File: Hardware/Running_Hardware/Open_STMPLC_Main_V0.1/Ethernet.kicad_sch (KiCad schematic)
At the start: 19 parts, among them J11 HY951180A, U7 LAN8720A, Y3 25MHz

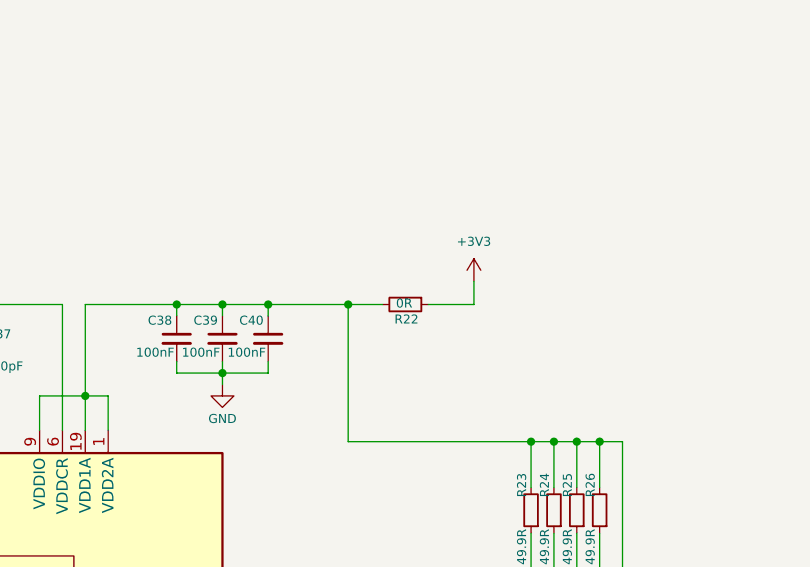
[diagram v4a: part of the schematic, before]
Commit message: Schematic updates
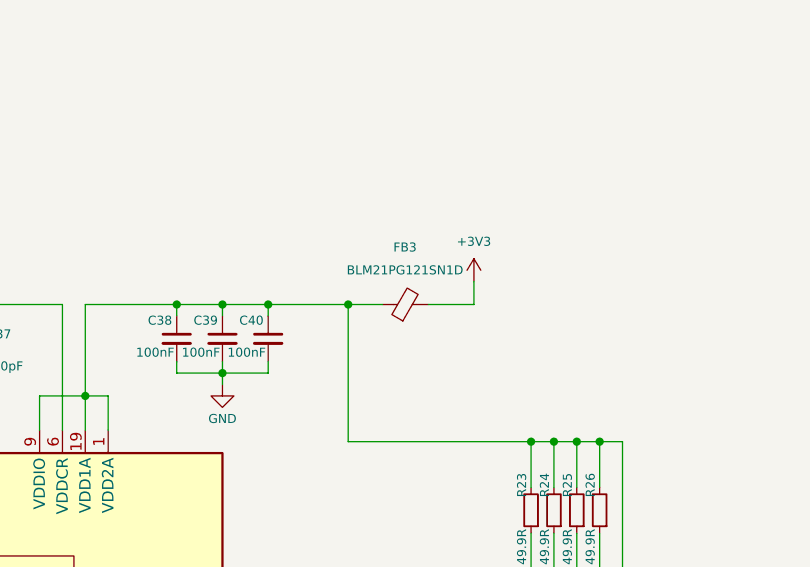
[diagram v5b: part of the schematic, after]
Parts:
- removed R22: 0R, Resistor_SMD:R_0603_1608Metric_Pad0.98x0.95mm_HandSolder, symbol Device:R_Small
- added FB3: BLM21PG121SN1D, Inductor_SMD:L_0805_2012Metric_Pad1.05x1.20mm_HandSolder, symbol Device:FerriteBead_Small
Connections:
- net +3V3: now also FB3.2
- net at C38.1, C39.1, C40.1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: now also FB3.1
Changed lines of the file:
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@@
+			)
+		)
+		(property "Sim.Pin" ""
+			(at 64.77 130.81 90)
+			(effects
+				(font
+					(size 1.27 1.27)
+				)
+				(hide yes)
 			)
 		)
@@
 			)
 		)
+		(property "Sim.Pin" ""
+			(at 127 58.42 0)
+			(effects
+				(font
+					(size 1.27 1.27)
+				)
+				(hide yes)
+			)
+		)
 		(pin "1"
 		)
@@
 		)
 		(property "Description" "Unpolarized capacitor, small symbol"
+			(at 95.25 59.69 0)
+			(effects
+				(font
+					(size 1.27 1.27)
+				)
+				(hide yes)
+			)
+		)
+		(property "Sim.Pin" ""
 			(at 95.25 59.69 0)
 			(effects
@@
 			)
 		)
+		(property "Sim.Pin" ""
+			(at 200.66 93.98 0)
+			(effects
+				(font
+					(size 1.27 1.27)
+				)
+				(hide yes)
+			)
+		)
 		(pin "6"
 		)
@@
 		(property "Description" "Resistor, small symbol"
 			(at 232.41 82.55 0)
+			(effects
+				(font
+					(size 1.27 1.27)
+				)
+				(hide yes)
+			)
+		)
+		(property "Sim.Pin" ""
+			(at 232.41 82.55 90)
 			(effects
 				(font
@@
 	)
 	(symbol
+		(lib_id "Device:FerriteBead_Small")
+		(at 147.32 54.61 90)
+		(unit 1)
+		(exclude_from_sim no)
+		(in_bom yes)
+		(on_board yes)
+		(dnp no)
+		(fields_autoplaced yes)
+		(property "Reference" "FB3"
+			(at 147.2819 48.26 90)
+			(effects
+				(font
+					(size 1 1)
+				)
+			)
+		)
+		(property "Value" "BLM21PG121SN1D"
+			(at 147.2819 50.8 90)
+			(effects
+				(font
+					(size 1 1)
+				)
+			)
+		)
+		(property "Footprint" "Inductor_SMD:L_0805_2012Metric_Pad1.05x1.20mm_HandSolder"
+			(at 147.32 56.388 90)
+			(effects
+				(font
+					(size 1.27 1.27)
+				)
+				(hide yes)
+			)
+		)
+		(property "Datasheet" "~"
+			(at 147.32 54.61 0)
+			(effects
+				(font
+					(size 1.27 1.27)
+				)
+				(hide yes)
+			)
+		)
+		(property "Description" "Ferrite bead, small symbol"
+			(at 147.32 54.61 0)
+			(effects
+				(font
+					(size 1.27 1.27)
+				)
+				(hide yes)
+			)
+		)
+		(pin "1"
+		)
+		(pin "2"
+		)
+		(instances
+			(project "Open_STMPLC_Main_V0.1"
+				(path "/0b17c9ff-697e-478a-b9b2-a0c5b14c9e6c/2c4ca765-43c3-4f95-8835-dba7f06999bb"
+					(reference "FB3")
+					(unit 1)
+				)
+			)
+		)
+	)
+	(symbol
 		(lib_id "Device:R_Small")
 		(at 168.91 77.47 180)
@@
 			)
 		)
+		(property "Sim.Pin" ""
+			(at 168.91 77.47 90)
+			(effects
+				(font
+					(size 1.27 1.27)
+				)
+				(hide yes)
+			)
+		)
 		(pin "2"
 		)
@@
 			)
 		)
+		(property "Sim.Pin" ""
+			(at 133.35 101.6 90)
+			(effects
+				(font
+					(size 1.27 1.27)
+				)
+				(hide yes)
+			)
+		)
 		(pin "2"
 		)
@@
 				(path "/0b17c9ff-697e-478a-b9b2-a0c5b14c9e6c/2c4ca765-43c3-4f95-8835-dba7f06999bb"
 					(reference "R21")
-					(unit 1)
-				)
-			)
-		)
-	)
-	(symbol
-		(lib_id "Device:R_Small")
-		(at 147.32 54.61 270)
-		(unit 1)
-		(exclude_from_sim no)
-		(in_bom yes)
-		(on_board yes)
-		(dnp no)
-		(property "Reference" "R22"
-			(at 147.447 56.261 90)
-			(effects
-				(font
-					(size 1 1)
-				)
-			)
-		)
-		(property "Value" "0R"
-			(at 147.193 54.483 90)
-			(effects
-				(font
-					(size 1 1)
-				)
-			)
-		)
-		(property "Footprint" "Resistor_SMD:R_0603_1608Metric_Pad0.98x0.95mm_HandSolder"
-			(at 147.32 54.61 0)
-			(effects
-				(font
-					(size 1.27 1.27)
-				)
-				(hide yes)
-			)
-		)
-		(property "Datasheet" "~"
-			(at 147.32 54.61 0)
-			(effects
-				(font
-					(size 1.27 1.27)
-				)
-				(hide yes)
-			)
-		)
-		(property "Description" "Resistor, small symbol"
-			(at 147.32 54.61 0)
-			(effects
-				(font
-					(size 1.27 1.27)
-				)
-				(hide yes)
-			)
-		)
-		(pin "2"
-		)
-		(pin "1"
-		)
-		(instances
-			(project "Open_STMPLC_Main_V0.1"
-				(path "/0b17c9ff-697e-478a-b9b2-a0c5b14c9e6c/2c4ca765-43c3-4f95-8835-dba7f06999bb"
-					(reference "R22")
 					(unit 1)
 				)
@@
 		(property "Description" "Resistor, small symbol"
 			(at 161.29 77.47 0)
+			(effects
+				(font
+					(size 1.27 1.27)
+				)
+				(hide yes)
+			)
+		)
+		(property "Sim.Pin" ""
+			(at 161.29 77.47 90)
 			(effects
 				(font
@@
 			)
 		)
+		(property "Sim.Pin" ""
+			(at 132.08 58.42 0)
+			(effects
+				(font
+					(size 1.27 1.27)
+				)
+				(hide yes)
+			)
+		)
 		(pin "1"
 		)
@@
 		(property "Description" "Resistor, small symbol"
 			(at 163.83 77.47 0)
+			(effects
+				(font
+					(size 1.27 1.27)
+				)
+				(hide yes)
+			)
+		)
+		(property "Sim.Pin" ""
+			(at 163.83 77.47 90)
 			(effects
 				(font
@@
 			)
 		)
+		(property "Sim.Pin" ""
+			(at 171.45 105.41 0)
+			(effects
+				(font
+					(size 1.27 1.27)
+				)
+				(hide yes)
+			)
+		)
 		(pin "1"
 		)
@@
 			)
 		)
+		(property "Sim.Pin" ""
+			(at 111.76 99.06 0)
+			(effects
+				(font
+					(size 1.27 1.27)
+				)
+				(hide yes)
+			)
+		)
 		(pin "18"
 		)
@@
 			)
 		)
+		(property "Sim.Pin" ""
+			(at 121.92 58.42 0)
+			(effects
+				(font
+					(size 1.27 1.27)
+				)
+				(hide yes)
+			)
+		)
 		(pin "1"
 		)
@@
 			)
 		)
+		(property "Sim.Pin" ""
+			(at 100.33 59.69 0)
+			(effects
+				(font
+					(size 1.27 1.27)
+				)
+				(hide yes)
+			)
+		)
 		(pin "1"
 		)
@@
 		(property "Description" "Resistor, small symbol"
 			(at 166.37 77.47 0)
+			(effects
+				(font
+					(size 1.27 1.27)
+				)
+				(hide yes)
+			)
+		)
+		(property "Sim.Pin" ""
+			(at 166.37 77.47 90)
 			(effects
 				(font
@@
 			)
 		)
+		(property "Sim.Pin" ""
+			(at 64.77 116.84 90)
+			(effects
+				(font
+					(size 1.27 1.27)
+				)
+				(hide yes)
+			)
+		)
 		(pin "1"
 		)
@@
 			)
 		)
+		(property "Sim.Pin" ""
+			(at 227.33 82.55 90)
+			(effects
+				(font
+					(size 1.27 1.27)
+				)
+				(hide yes)
+			)
+		)
 		(pin "2"
 		)
@@
 			(effects
 				(font
+					(size 1.27 1.27)
+				)
+				(hide yes)
+			)
+		)
+		(property "Sim.Pin" ""
+			(at 69.85 124.46 90)
+			(effects
+				(font

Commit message: Component placement main pcb
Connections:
- net ETH_~{INT} renamed ETH_REFCLKO
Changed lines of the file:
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@@
 		)
 	)
-	(hierarchical_label "ETH_~{INT}"
+	(hierarchical_label "ETH_REFCLKO"
 		(shape output)
 		(at 90.17 111.76 180)

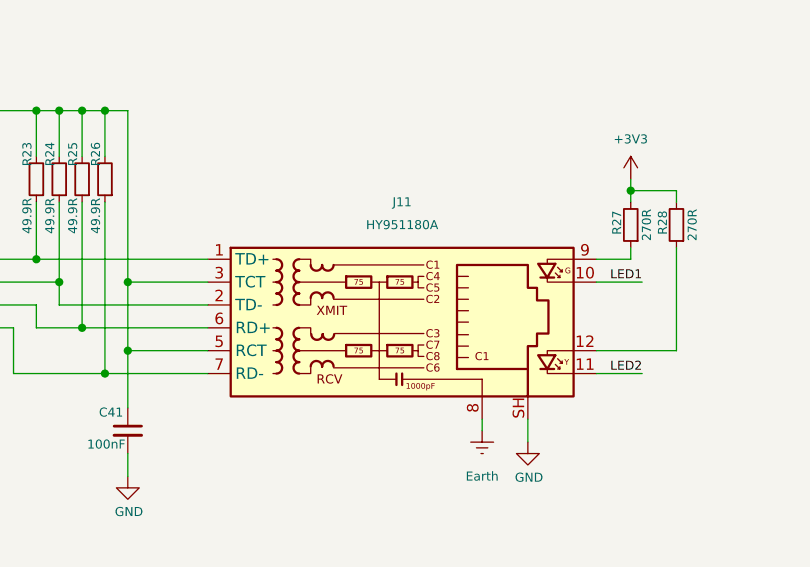
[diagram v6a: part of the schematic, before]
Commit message: IO board layout completion and DRC clear
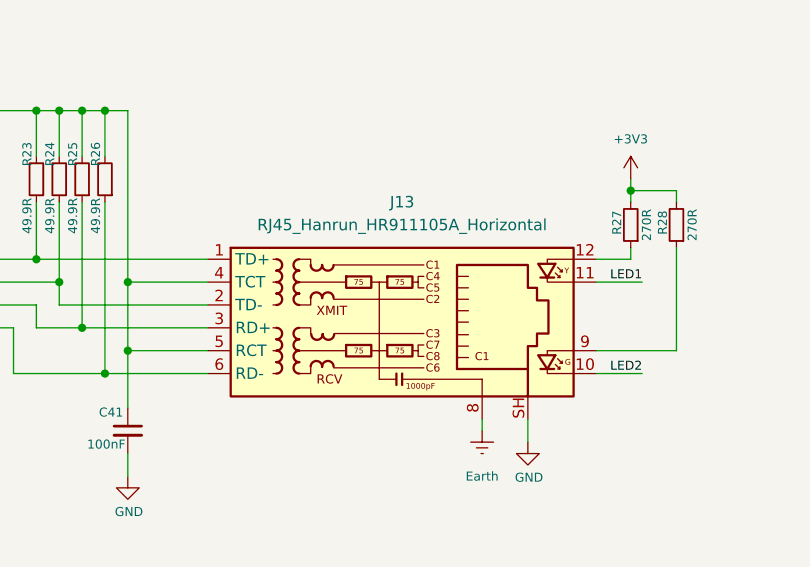
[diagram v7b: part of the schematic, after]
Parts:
- removed J11: HY951180A, HY951180A:HY951180A, symbol HY951180A:HY951180A
- added J13: RJ45_Hanrun_HR911105A_Horizontal, Connector_RJ:RJ45_Hanrun_HR911105A_Horizontal, symbol Connector:RJ45_Hanrun_HR911105A_Horizontal
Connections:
- net Earth: now also J13.8
- net GND: now also J13.SH
- net LED1: now also J13.11
- net LED2: now also J13.10
- net at C38.1, C39.1, C40.1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: now also J13.4 (TCT), J13.5 (RCT)
- net at R23.1, U7.21 (TXP): now also J13.1 (TD+)
- net at R28.1: now also J13.9
- net at R24.1, U7.20 (TXN): now also J13.2 (TD-)
- net at R25.1, U7.23 (RXP): now also J13.3 (RD+)
- net at R26.1, U7.22 (RXN): now also J13.6 (RD-)
- net at R27.1: now also J13.12
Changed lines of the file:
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@@
-	)
-	(symbol
-		(lib_id "HY951180A:HY951180A")
-		(at 200.66 93.98 0)
-		(unit 1)
-		(exclude_from_sim no)
-		(in_bom yes)
-		(on_board yes)
-		(dnp no)
-		(fields_autoplaced yes)
-		(property "Reference" "J11"
-			(at 201.93 80.01 0)
-			(effects
-				(font
-					(size 1 1)
-				)
-			)
-		)
-		(property "Value" "HY951180A"
-			(at 201.93 82.55 0)
-			(effects
-				(font
-					(size 1 1)
-				)
-			)
-		)
-		(property "Footprint" "HY951180A:HY951180A"
-			(at 200.66 81.28 0)
-			(effects
-				(font
-					(size 1.27 1.27)
-				)
-				(hide yes)
-			)
-		)
-		(property "Datasheet" ""
-			(at 200.66 78.74 0)
-			(effects
-				(font
-					(size 1.27 1.27)
-				)
-				(hide yes)
-			)
-		)
-		(property "Description" ""
-			(at 200.66 93.98 0)
-			(effects
-				(font
-					(size 1.27 1.27)
-				)
-				(hide yes)
-			)
-		)
-		(property "Sim.Pin" ""
-			(at 200.66 93.98 0)
-			(effects
-				(font
-					(size 1.27 1.27)
-				)
-				(hide yes)
-			)
-		)
-		(pin "6"
-		)
-		(pin "7"
-		)
-		(pin "2"
-		)
-		(pin "5"
-		)
-		(pin "9"
-		)
-		(pin "1"
-		)
-		(pin "11"
-		)
-		(pin "10"
-		)
-		(pin "3"
-		)
-		(pin "12"
-		)
-		(pin "8"
-		)
-		(pin "SH"
-		)
-		(pin "4"
-		)
-		(instances
-			(project "Open_STMPLC_Main_V0.1"
-				(path "/0b17c9ff-697e-478a-b9b2-a0c5b14c9e6c/2c4ca765-43c3-4f95-8835-dba7f06999bb"
-					(reference "J11")
-					(unit 1)
-				)
-			)
-		)
 	)
 	(symbol
@@
 					(unit 1)
 				)
+			)
+		)
+	)
+	(symbol
+		(lib_id "Connector:RJ45_Hanrun_HR911105A_Horizontal")
+		(at 200.66 93.98 0)
+		(unit 1)
+		(exclude_from_sim no)
+		(in_bom yes)
+		(on_board yes)
+		(dnp no)
+		(fields_autoplaced yes)
+		(property "Reference" "J13"
+			(at 201.93 80.01 0)
+			(effects
+				(font
+					(size 1.27 1.27)
+				)
+			)
+		)
+		(property "Value" "RJ45_Hanrun_HR911105A_Horizontal"
+			(at 201.93 82.55 0)
+			(effects
+				(font
+					(size 1.27 1.27)
+				)
+			)
+		)
+		(property "Footprint" "Connector_RJ:RJ45_Hanrun_HR911105A_Horizontal"
+			(at 200.66 81.28 0)
+			(effects
+				(font
+					(size 1.27 1.27)
+				)
+				(hide yes)
+			)
+		)
+		(property "Datasheet" "https://datasheet.lcsc.com/lcsc/1811141815_HANRUN-Zhongshan-HanRun-Elec-HR911105A_C12074.pdf"
+			(at 200.66 78.74 0)
+			(effects
+				(font
+					(size 1.27 1.27)
+				)
+				(hide yes)
+			)
+		)
+		(property "Description" "1 Port RJ45 Magjack Connector Through Hole 10/100 Base-T, AutoMDIX"
+			(at 200.66 93.98 0)
+			(effects
+				(font
+					(size 1.27 1.27)
+				)
+				(hide yes)
+			)
+		)
+		(pin "12"
+		)
+		(pin "9"
+		)
+		(pin "7"
+		)
+		(pin "3"
+		)
+		(pin "2"
+		)
+		(pin "6"
+		)
+		(pin "SH"
+		)
+		(pin "11"
+		)
+		(pin "5"
+		)
+		(pin "10"
+		)
+		(pin "1"
+		)
+		(pin "8"
+		)
+		(pin "4"
+		)
+		(instances
+			(project ""
+				(path "/0b17c9ff-697e-478a-b9b2-a0c5b14c9e6c/2c4ca765-43c3-4f95-8835-dba7f06999bb"
+					(reference "J13")
+					(unit 1)
+				)

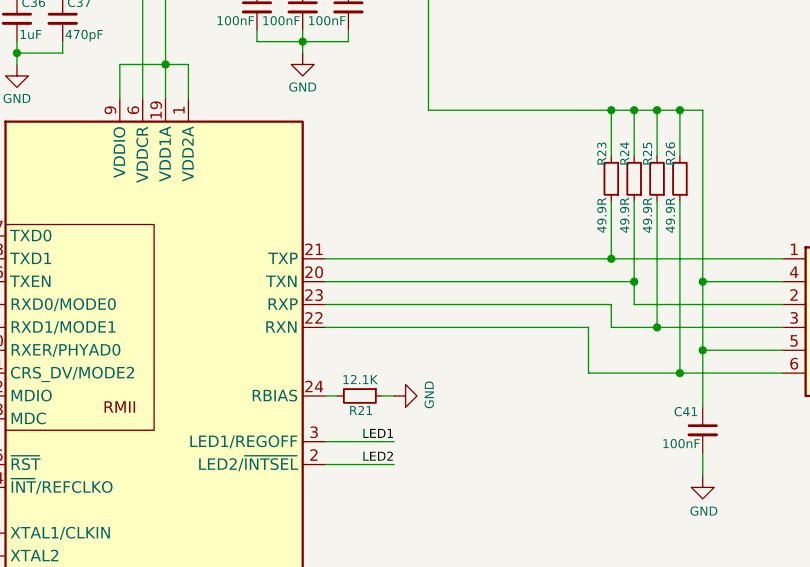
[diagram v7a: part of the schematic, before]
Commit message: Layer stack up main PCB and pin mapping
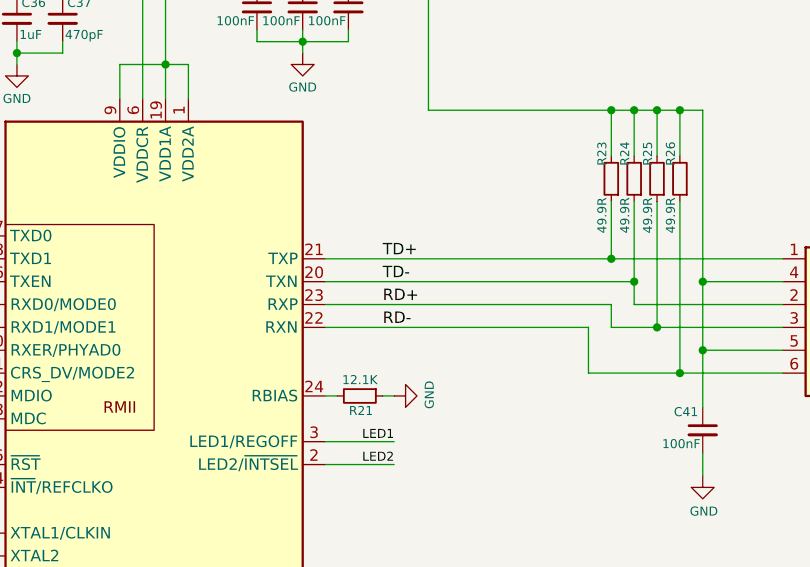
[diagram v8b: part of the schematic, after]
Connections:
- net RD-: now reaches J13.6 (RD-), R26.1, U7.22 (RXN)
- net TD+: now reaches J13.1 (TD+), R23.1, U7.21 (TXP)
- net TD-: now reaches J13.2 (TD-), R24.1, U7.20 (TXN)
- net RD+: now reaches J13.3 (RD+), R25.1, U7.23 (RXP)
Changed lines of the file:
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@@
+		)
+	)
+	(label "TD-"
+		(at 135.89 88.9 0)
+		(effects
+			(font
+				(size 1.27 1.27)
+			)
+			(justify left bottom)
+		)
+	)
+	(label "RD+"
+		(at 135.89 91.44 0)
+		(effects
+			(font
+				(size 1.27 1.27)
+			)
+			(justify left bottom)
 		)
 	)
@@
 		)
 	)
+	(label "TD+"
+		(at 135.89 86.36 0)
+		(effects
+			(font
+				(size 1.27 1.27)
+			)
+			(justify left bottom)
+		)
+	)
 	(label "LED1"
 		(at 137.16 106.68 180)
@@
 			)
 			(justify right bottom)
+		)
+	)
+	(label "RD-"
+		(at 135.89 93.98 0)
+		(effects
+			(font
+				(size 1.27 1.27)
+			)
+			(justify left bottom)
 		)
 	)
@@
 		)
 		(instances
-			(project ""
+			(project "Open_STMPLC_Main_V0.1"
 				(path "/0b17c9ff-697e-478a-b9b2-a0c5b14c9e6c/2c4ca765-43c3-4f95-8835-dba7f06999bb"
 					(reference "J13")
